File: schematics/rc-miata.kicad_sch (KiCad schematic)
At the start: 8 parts, among them M1 BLDC_MOTOR, M2 22KG SERVO, U2 UBEC, U3 ESC, U4 ESP32 DEVKITV1

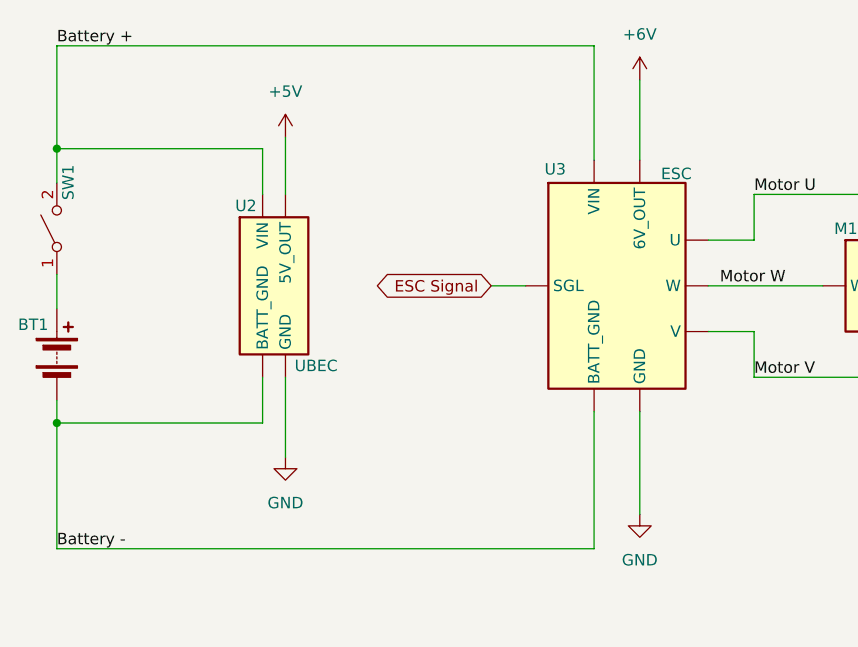
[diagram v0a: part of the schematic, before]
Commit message: Fixed ERC Errors
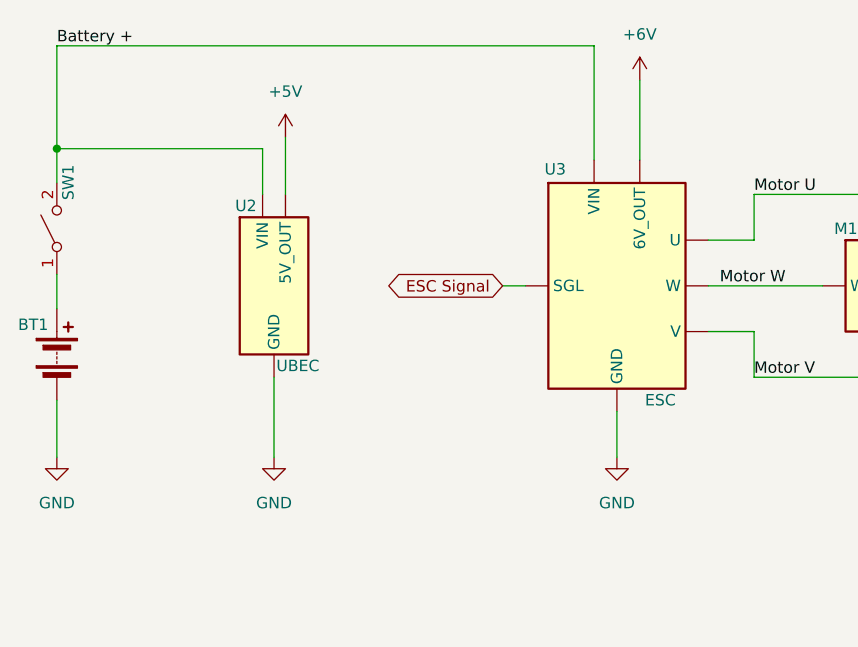
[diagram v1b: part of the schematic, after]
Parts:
- C1: footprint (none) -> Capacitor_THT:CP_Radial_D10.0mm_P2.50mm
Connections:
- net GND: now also BT1.2 (-)
- removed net Battery -: BT1.2 (-), U2.2 (BATT_GND), U3.2 (BATT_GND)
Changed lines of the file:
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@@
-	)
-	(junction
-		(at 43.18 110.49)
-		(diameter 0)
-		(color 0 0 0 0)
 	)
 	(junction
@@
 	(wire
 		(pts
-			(xy 43.18 110.49) (xy 43.18 124.46)
-		)
-		(stroke
-			(width 0)
-			(type default)
-		)
-	)
-	(wire
-		(pts
 			(xy 43.18 68.58) (xy 102.87 68.58)
 		)
@@
 	(wire
 		(pts
-			(xy 68.58 105.41) (xy 68.58 114.3)
-		)
-		(stroke
-			(width 0)
-			(type default)
-		)
-	)
-	(wire
-		(pts
 			(xy 68.58 78.74) (xy 68.58 85.09)
 		)
@@
 	(wire
 		(pts
-			(xy 107.95 109.22) (xy 107.95 120.65)
-		)
-		(stroke
-			(width 0)
-			(type default)
-		)
-	)
-	(wire
-		(pts
 			(xy 43.18 83.82) (xy 43.18 80.01)
 		)
@@
 	(wire
 		(pts
-			(xy 66.04 110.49) (xy 66.04 105.41)
-		)
-		(stroke
-			(width 0)
-			(type default)
-		)
-	)
-	(wire
-		(pts
 			(xy 165.1 76.2) (xy 165.1 73.66)
 		)
@@
 	(wire
 		(pts
-			(xy 43.18 110.49) (xy 66.04 110.49)
-		)
-		(stroke
-			(width 0)
-			(type default)
-		)
-	)
-	(wire
-		(pts
-			(xy 95.25 95.25) (xy 91.44 95.25)
+			(xy 95.25 95.25) (xy 92.71 95.25)
 		)
 		(stroke
@@
 	(wire
 		(pts
-			(xy 102.87 109.22) (xy 102.87 124.46)
-		)
-		(stroke
-			(width 0)
-			(type default)
-		)
-	)
-	(wire
-		(pts
-			(xy 102.87 124.46) (xy 43.18 124.46)
+			(xy 105.41 109.22) (xy 105.41 114.3)
 		)
 		(stroke
@@
 	(wire
 		(pts
-			(xy 43.18 107.95) (xy 43.18 110.49)
+			(xy 43.18 107.95) (xy 43.18 114.3)
 		)
 		(stroke
@@
 		(pts
 			(xy 165.1 63.5) (xy 180.34 63.5)
+		)
+		(stroke
+			(width 0)
+			(type default)
+		)
+	)
+	(wire
+		(pts
+			(xy 67.31 105.41) (xy 67.31 114.3)
 		)
 		(stroke
@@
 	(label "Motor U"
 		(at 120.65 85.09 0)
-		(effects
-			(font
-				(size 1.27 1.27)
-			)
-			(justify left bottom)
-		)
-	)
-	(label "Battery -"
-		(at 43.18 124.46 0)
 		(effects
 			(font
@@
 	(global_label "ESC Signal"
 		(shape bidirectional)
-		(at 91.44 95.25 180)
+		(at 92.71 95.25 180)
 		(fields_autoplaced yes)
 		(effects
@@
 		)
 		(property "Intersheetrefs" "${INTERSHEET_REFS}"
-			(at 76.8209 95.25 0)
+			(at 78.0909 95.25 0)
 			(hide yes)
 			(show_name no)
@@
 			)
 		)
-		(property "Footprint" ""
+		(property "Footprint" "Capacitor_THT:CP_Radial_D10.0mm_P2.50mm"
 			(at 165.1 69.85 0)
 			(hide yes)
@@
 	(symbol
 		(lib_id "power:GND")
-		(at 68.58 114.3 0)
+		(at 67.31 114.3 0)
 		(unit 1)
 		(body_style 1)
@@
 		(fields_autoplaced yes)
 		(property "Reference" "#PWR01"
-			(at 68.58 120.65 0)
+			(at 67.31 120.65 0)
 			(hide yes)
 			(show_name no)
@@
 		)
 		(property "Value" "GND"
-			(at 68.58 119.38 0)
+			(at 67.31 119.38 0)
 			(show_name no)
 			(do_not_autoplace no)
@@
 		)
 		(property "Footprint" ""
-			(at 68.58 114.3 0)
+			(at 67.31 114.3 0)
 			(hide yes)
 			(show_name no)
@@
 		)
 		(property "Datasheet" ""
-			(at 68.58 114.3 0)
+			(at 67.31 114.3 0)
 			(hide yes)
 			(show_name no)
@@
 		)
 		(property "Description" "Power symbol creates a global label with name \"GND\" , ground"
-			(at 68.58 114.3 0)
+			(at 67.31 114.3 0)
 			(hide yes)
 			(show_name no)
@@
 				(path "/59cbdaad-7c89-4958-b9bb-08b035442600"
 					(reference "#PWR01")
+					(unit 1)
+				)
+			)
+		)
+	)
+	(symbol
+		(lib_id "power:GND")
+		(at 43.18 114.3 0)
+		(unit 1)
+		(body_style 1)
+		(exclude_from_sim no)
+		(in_bom yes)
+		(on_board yes)
+		(in_pos_files yes)
+		(dnp no)
+		(fields_autoplaced yes)
+		(property "Reference" "#PWR010"
+			(at 43.18 120.65 0)
+			(hide yes)
+			(show_name no)
+			(do_not_autoplace no)
+			(effects
+				(font
+					(size 1.27 1.27)
+				)
+			)
+		)
+		(property "Value" "GND"
+			(at 43.18 119.38 0)
+			(show_name no)
+			(do_not_autoplace no)
+			(effects
+				(font
+					(size 1.27 1.27)
+				)
+			)
+		)
+		(property "Footprint" ""
+			(at 43.18 114.3 0)
+			(hide yes)
+			(show_name no)
+			(do_not_autoplace no)
+			(effects
+				(font
+					(size 1.27 1.27)
+				)
+			)
+		)
+		(property "Datasheet" ""
+			(at 43.18 114.3 0)
+			(hide yes)
+			(show_name no)
+			(do_not_autoplace no)
+			(effects
+				(font
+					(size 1.27 1.27)
+				)
+			)
+		)
+		(property "Description" "Power symbol creates a global label with name \"GND\" , ground"
+			(at 43.18 114.3 0)
+			(hide yes)
+			(show_name no)
+			(do_not_autoplace no)
+			(effects
+				(font
+					(size 1.27 1.27)
+				)
+			)
+		)
+		(pin "1"
+		)
+		(instances
+			(project "rc-miata"
+				(path "/59cbdaad-7c89-4958-b9bb-08b035442600"
+					(reference "#PWR010")
 					(unit 1)
 				)
@@
 		)
 		(property "Value" "UBEC"
-			(at 69.596 104.14 0)
+			(at 67.564 104.14 0)
 			(show_name no)
 			(do_not_autoplace no)
@@
 		)
 		(pin "1"
-		)
-		(pin "2"
 		)
 		(pin "4"
@@
 		)
 		(property "Value" "ESC"
-			(at 112.014 82.804 0)
+			(at 110.236 107.95 0)
 			(show_name no)
 			(do_not_autoplace no)
@@
 		)
 		(pin "4"
-		)
-		(pin "2"
 		)
 		(pin "6"
@@
 	(symbol
 		(lib_id "power:GND")
-		(at 107.95 120.65 0)
+		(at 105.41 114.3 0)
 		(unit 1)
 		(body_style 1)
@@
 		(fields_autoplaced yes)
 		(property "Reference" "#PWR03"
-			(at 107.95 127 0)
+			(at 105.41 120.65 0)
 			(hide yes)
 			(show_name no)
@@
 		)
 		(property "Value" "GND"
-			(at 107.95 125.73 0)
+			(at 105.41 119.38 0)
 			(show_name no)
 			(do_not_autoplace no)
@@
 		)
 		(property "Footprint" ""
-			(at 107.95 120.65 0)
+			(at 105.41 114.3 0)
 			(hide yes)
 			(show_name no)
@@
 		)
 		(property "Datasheet" ""
-			(at 107.95 120.65 0)
+			(at 105.41 114.3 0)
 			(hide yes)
 			(show_name no)
@@
 		)
 		(property "Description" "Power symbol creates a global label with name \"GND\" , ground"
-			(at 107.95 120.65 0)
-			(hide yes)
-			(show_name no)
+			(at 105.41 114.3 0)
+			(hide yes)
+			(show_name no)

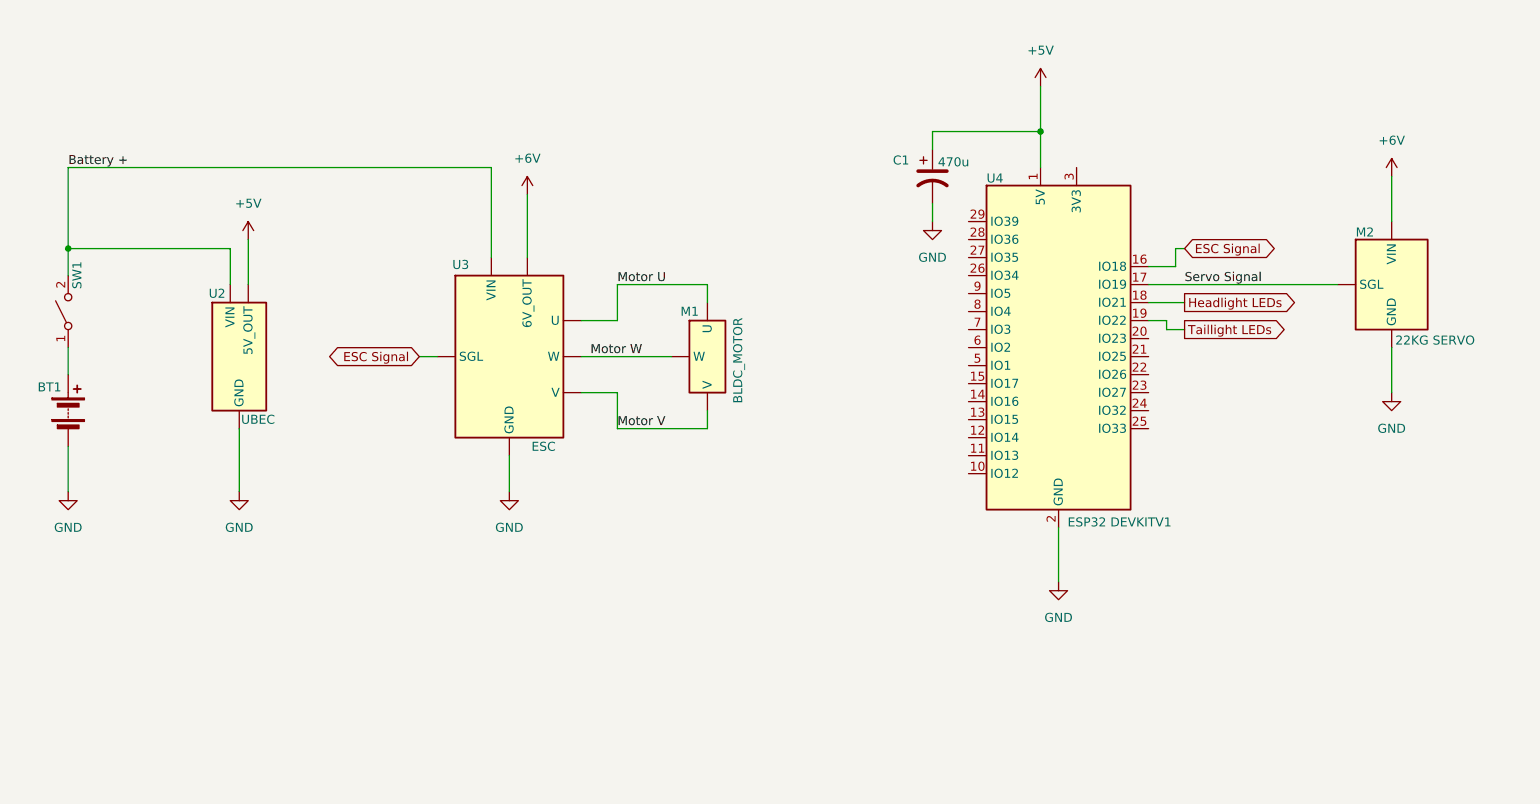
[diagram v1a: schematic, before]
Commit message: Added and Wired LEDs. Changed sheet to US LETTER SIZE A
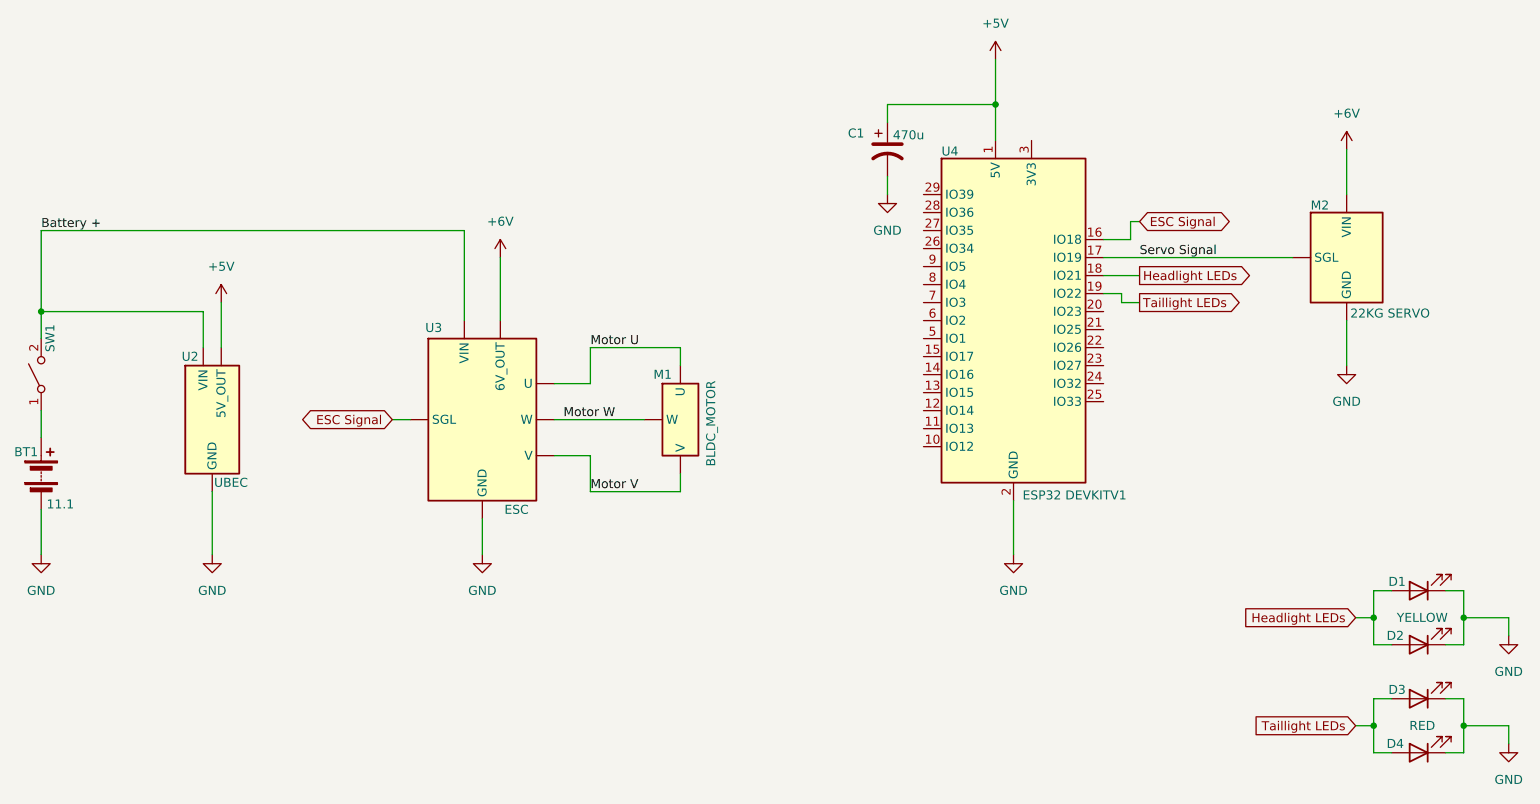
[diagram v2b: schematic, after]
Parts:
- added D1, D2, D4: YELLOW, symbol Device:LED
- added D3: RED, symbol Device:LED
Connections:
- net GND: now also D1.1 (K), D2.1 (K), D3.1 (K), D4.1 (K)
- net Headlight LEDs: now also D1.2 (A), D2.2 (A)
- net Taillight LEDs: now also D3.2 (A), D4.2 (A)
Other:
- moved on the sheet: C1, M1, M2, SW1, U2, U3, U4

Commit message: Added Resistors for LEDs. Value Clarity
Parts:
- added R1, R2: 330, symbol Device:R_US
- BT1: value 11.1 -> 11V1
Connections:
- net Headlight LEDs: now also R1.2; no longer D1.2 (A), D2.2 (A)
- net Taillight LEDs: now also R2.2; no longer D3.2 (A), D4.2 (A)
- new net: D1.2 (A), D2.2 (A), R1.1
- new net: D3.2 (A), D4.2 (A), R2.1
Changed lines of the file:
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@@
+	)
+	(junction
+		(at 227.33 147.32)
+		(diameter 0)
+		(color 0 0 0 0)
+	)
+	(junction
+		(at 173.99 59.69)
+		(diameter 0)
+		(color 0 0 0 0)
 	)
 	(junction
@@
 	)
 	(junction
-		(at 173.99 59.69)
-		(diameter 0)
-		(color 0 0 0 0)
-	)
-	(junction
-		(at 227.33 147.32)
-		(diameter 0)
-		(color 0 0 0 0)
-	)
-	(junction
 		(at 240.03 132.08)
 		(diameter 0)
@@
 	(wire
 		(pts
+			(xy 224.79 147.32) (xy 227.33 147.32)
+		)
+		(stroke
+			(width 0)
+			(type default)
+		)
+	)
+	(wire
+		(pts
 			(xy 240.03 132.08) (xy 240.03 135.89)
 		)
@@
 	(wire
 		(pts
+			(xy 224.79 132.08) (xy 227.33 132.08)
+		)
+		(stroke
+			(width 0)
+			(type default)
+		)
+	)
+	(wire
+		(pts
 			(xy 104.14 90.17) (xy 104.14 81.28)
 		)
@@
 	(wire
 		(pts
-			(xy 224.79 132.08) (xy 227.33 132.08)
+			(xy 214.63 132.08) (xy 217.17 132.08)
 		)
 		(stroke
@@
 	(wire
 		(pts
-			(xy 224.79 147.32) (xy 227.33 147.32)
+			(xy 214.63 147.32) (xy 217.17 147.32)
 		)
 		(stroke
@@
 	(global_label "Taillight LEDs"
 		(shape input)
-		(at 224.79 147.32 180)
+		(at 214.63 147.32 180)
 		(fields_autoplaced yes)
 		(effects
@@
 		)
 		(property "Intersheetrefs" "${INTERSHEET_REFS}"
-			(at 208.6817 147.32 0)
+			(at 198.5217 147.32 0)
 			(hide yes)
 			(show_name no)
@@
 	(global_label "Headlight LEDs"
 		(shape input)
-		(at 224.79 132.08 180)
+		(at 214.63 132.08 180)
 		(fields_autoplaced yes)
 		(effects
@@
 		)
 		(property "Intersheetrefs" "${INTERSHEET_REFS}"
-			(at 207.3512 132.08 0)
+			(at 197.1912 132.08 0)
 			(hide yes)
 			(show_name no)
@@
 	)
 	(symbol
+		(lib_id "Device:R_US")
+		(at 220.98 132.08 270)
+		(unit 1)
+		(body_style 1)
+		(exclude_from_sim no)
+		(in_bom yes)
+		(on_board yes)
+		(in_pos_files yes)
+		(dnp no)
+		(property "Reference" "R1"
+			(at 216.916 130.81 90)
+			(show_name no)
+			(do_not_autoplace no)
+			(effects
+				(font
+					(size 1.27 1.27)
+				)
+			)
+		)
+		(property "Value" "330"
+			(at 221.488 134.874 90)
+			(show_name no)
+			(do_not_autoplace no)
+			(effects
+				(font
+					(size 1.27 1.27)
+				)
+			)
+		)
+		(property "Footprint" ""
+			(at 220.726 133.096 90)
+			(hide yes)
+			(show_name no)
+			(do_not_autoplace no)
+			(effects
+				(font
+					(size 1.27 1.27)
+				)
+			)
+		)
+		(property "Datasheet" ""
+			(at 220.98 132.08 0)
+			(hide yes)
+			(show_name no)
+			(do_not_autoplace no)
+			(effects
+				(font
+					(size 1.27 1.27)
+				)
+			)
+		)
+		(property "Description" "Resistor, US symbol"
+			(at 220.98 132.08 0)
+			(hide yes)
+			(show_name no)
+			(do_not_autoplace no)
+			(effects
+				(font
+					(size 1.27 1.27)
+				)
+			)
+		)
+		(pin "2"
+		)
+		(pin "1"
+		)
+		(instances
+			(project "rc-miata"
+				(path "/59cbdaad-7c89-4958-b9bb-08b035442600"
+					(reference "R1")
+					(unit 1)
+				)
+			)
+		)
+	)
+	(symbol
+		(lib_id "Device:R_US")
+		(at 220.98 147.32 270)
+		(unit 1)
+		(body_style 1)
+		(exclude_from_sim no)
+		(in_bom yes)
+		(on_board yes)
+		(in_pos_files yes)
+		(dnp no)
+		(property "Reference" "R2"
+			(at 216.916 146.05 90)
+			(show_name no)
+			(do_not_autoplace no)
+			(effects
+				(font
+					(size 1.27 1.27)
+				)
+			)
+		)
+		(property "Value" "330"
+			(at 221.488 149.86 90)
+			(show_name no)
+			(do_not_autoplace no)
+			(effects
+				(font
+					(size 1.27 1.27)
+				)
+			)
+		)
+		(property "Footprint" ""
+			(at 220.726 148.336 90)
+			(hide yes)
+			(show_name no)
+			(do_not_autoplace no)
+			(effects
+				(font
+					(size 1.27 1.27)
+				)
+			)
+		)
+		(property "Datasheet" ""
+			(at 220.98 147.32 0)
+			(hide yes)
+			(show_name no)
+			(do_not_autoplace no)
+			(effects
+				(font
+					(size 1.27 1.27)
+				)
+			)
+		)
+		(property "Description" "Resistor, US symbol"
+			(at 220.98 147.32 0)
+			(hide yes)
+			(show_name no)
+			(do_not_autoplace no)
+			(effects
+				(font
+					(size 1.27 1.27)
+				)
+			)
+		)
+		(pin "2"
+		)
+		(pin "1"
+		)
+		(instances
+			(project "rc-miata"
+				(path "/59cbdaad-7c89-4958-b9bb-08b035442600"
+					(reference "R2")
+					(unit 1)
+				)
+			)
+		)
+	)
+	(symbol
 		(lib_id "power:GND")
 		(at 63.5 123.19 0)
@@
 			)
 		)
-		(property "Value" "11.1"
+		(property "Value" "11V1"
 			(at 40.132 116.078 0)
 			(show_name no)
